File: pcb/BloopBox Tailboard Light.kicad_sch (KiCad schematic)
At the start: 14 parts, among them J1 Mainboard, J2 USB_C_Receptacle_Power, SW1 Button1, SW2 Button2

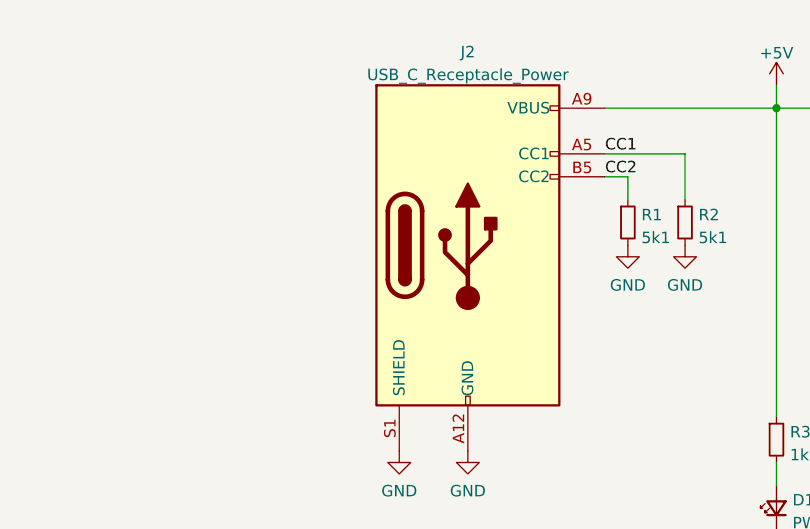
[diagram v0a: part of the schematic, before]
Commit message: chore: update to KiCad 8
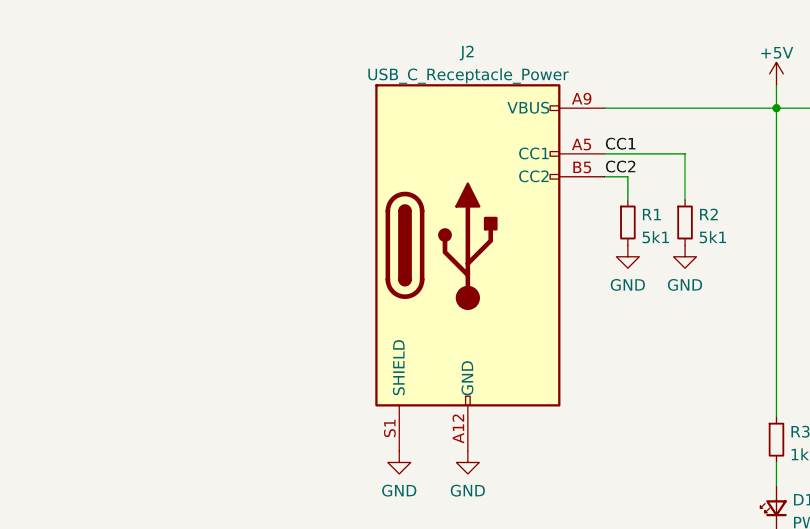
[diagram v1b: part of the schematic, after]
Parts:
- H1, H2: footprint MountingHole:MountingHole_3.2mm_M3_Pad -> MountingHole:MountingHole_3.2mm_M3

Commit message: fix: part number for connector
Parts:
- J1: LCSC C14531 -> C20598766
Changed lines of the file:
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@@
 			)
 		)
-		(property "LCSC" "C14531"
+		(property "LCSC" "C20598766"
 			(at 114.3 46.99 0)
 			(effects
